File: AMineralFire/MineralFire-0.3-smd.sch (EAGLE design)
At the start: 86 parts, among them IC1 LM358, Q1 20MHz, Q2 20MHz, Q3 2N3906, Q4 2N3906, Q5 2N3906, Q6 2N3906, Q7 2N3906, Q8 2N3906, Q9 2N3906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

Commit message: Updated to almost all SMD
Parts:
- removed IC1: LM358, SparkFun-IC-Amplifiers:LM358
- removed V1: 7409N, 74ttl-din:7409N
- added IC2: 74LS09D, 74xx-eu:74LS09D
- added IC3: LM358D, linear:LM358D
- C14, C6: device rcl:C-EU075-032X103 -> rcl:C-USC0805K
- C4, C5, C7: device SparkFun-Capacitors:10UF-POLAR-RADIAL-2.5MM-25V-20% -> rcl:CPOL-US153CLV-0505
- D1, D2, D3, D4: device SparkFun-DiscreteSemi:DIODE-1N4148 -> adafruit:DIODESMA
- Q1, Q2: device adafruit:CRYSTALHC49U70 -> adafruit:CRYSTALHC49UP
- Q3, Q4, Q5, Q6, Q7, Q8, Q9: value 2N3906 -> MMBT3906LT1SMD; device transistor-pnp:2N3906 -> transistor-pnp:MMBT3906LT1SMD
- T1, T2, T3, T4, T5: device SparkFun-DiscreteSemi:TRANS_NPN-2N3904 -> transistor:MMBT3904LT1-NPN-SOT23-BEC
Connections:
- net +12V: no longer IC1G3.P$V+
- net +5V: now also IC2P.VCC, IC3P.V+; no longer V1/+UB.+UB
- net BUTLED: now also IC3B.-IN; no longer IC1G2.+IN
- net GND: now also IC2P.GND, IC3P.V-; no longer IC1G3.P$V-, V1/-UB.-UB
- net LBUTTON: now also IC2A.I1; no longer V1/1.B
- net LTRIG: now also IC2A.I0; no longer V1/1.A
- net N$19: now also IC3B.OUT; no longer IC1G2.OUT
- net N$24: now also IC3B.+IN; no longer IC1G2.-IN
- net N$32: now also IC3A.+IN; no longer IC1G1.-IN
- net N$33: now also IC3A.OUT; no longer IC1G1.OUT
- net TRIG: now also IC2A.O; no longer V1/1.Y
- net TRIGO: now also IC3A.-IN; no longer IC1G1.+IN

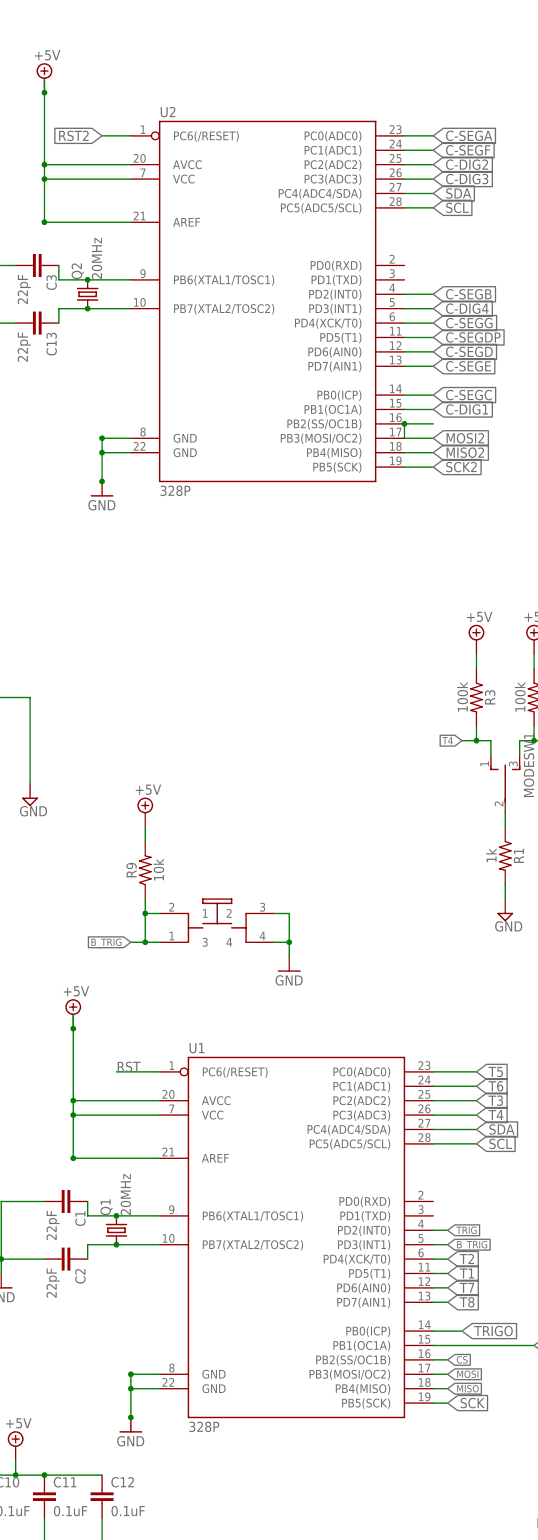
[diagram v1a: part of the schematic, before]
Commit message: 0.3-smd nor fully smd
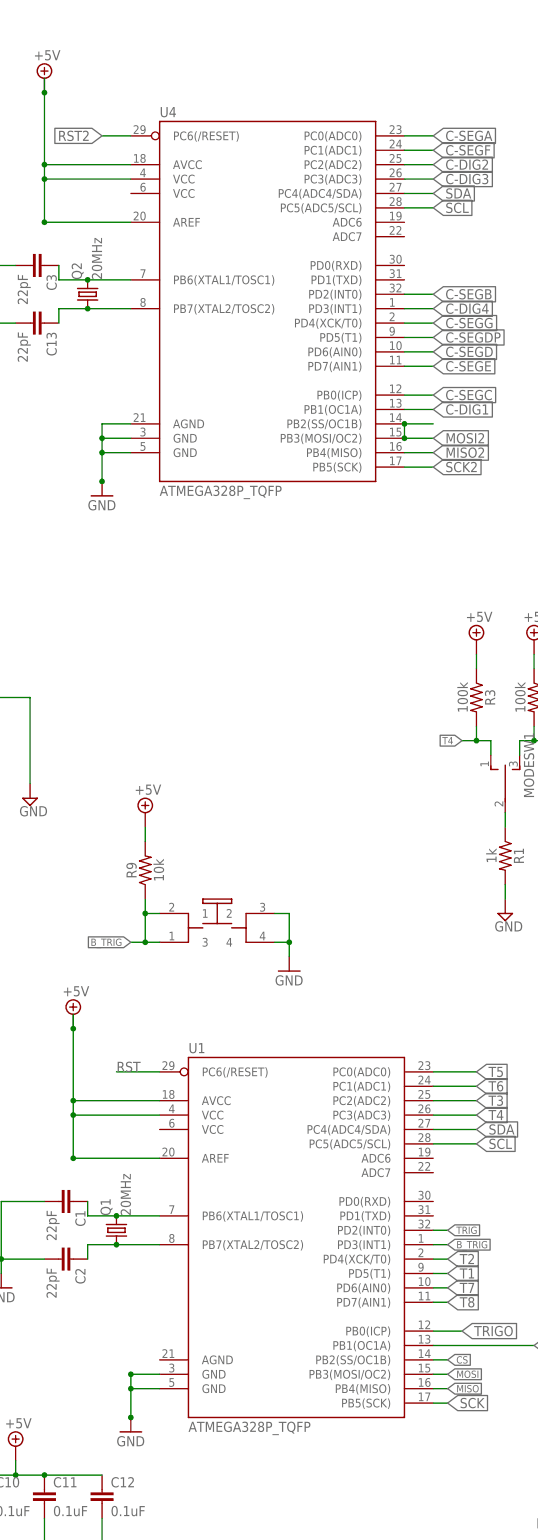
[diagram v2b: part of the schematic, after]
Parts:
- removed U2: 328P, SparkFun-IC-Microcontroller:ATMEGA328P_PDIP
- added U4: ATMEGA328P_TQFP, SparkFun-IC-Microcontroller:ATMEGA328P_TQFP
- U1: value 328P -> ATMEGA328P_TQFP; device SparkFun-IC-Microcontroller:ATMEGA328P_PDIP -> SparkFun-IC-Microcontroller:ATMEGA328P_TQFP
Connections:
- net +5V: now also U1.VCC@4, U4.AREF, U4.AVCC, U4.VCC@4; no longer U1.VCC, U2.AREF, U2.AVCC, U2.VCC
- net C-DIG1: now also U4.PB1(OC1A); no longer U2.PB1(OC1A)
- net C-DIG2: now also U4.PC2(ADC2); no longer U2.PC2(ADC2)
- net C-DIG3: now also U4.PC3(ADC3); no longer U2.PC3(ADC3)
- net C-DIG4: now also U4.PD3(INT1); no longer U2.PD3(INT1)
- net C-SEGA: now also U4.PC0(ADC0); no longer U2.PC0(ADC0)
- net C-SEGB: now also U4.PD2(INT0); no longer U2.PD2(INT0)
- net C-SEGC: now also U4.PB0(ICP); no longer U2.PB0(ICP)
- net C-SEGD: now also U4.PD6(AIN0); no longer U2.PD6(AIN0)
- net C-SEGDP: now also U4.PD5(T1); no longer U2.PD5(T1)
- net C-SEGE: now also U4.PD7(AIN1); no longer U2.PD7(AIN1)
- net C-SEGF: now also U4.PC1(ADC1); no longer U2.PC1(ADC1)
- net C-SEGG: now also U4.PD4(XCK/T0); no longer U2.PD4(XCK/T0)
- net GND: now also U1.GND@3, U1.GND@5, U4.AGND, U4.GND@3, U4.GND@5; no longer U1.GND@1, U1.GND@2, U2.GND@1, U2.GND@2
- net MISO2: now also U4.PB4(MISO); no longer U2.PB4(MISO)
- net MOSI2: now also U4.PB2(SS/OC1B), U4.PB3(MOSI/OC2); no longer U2.PB2(SS/OC1B), U2.PB3(MOSI/OC2)
- net N$7: now also U4.PB6(XTAL1/TOSC1); no longer U2.PB6(XTAL1/TOSC1)
- net N$8: now also U4.PB7(XTAL2/TOSC2); no longer U2.PB7(XTAL2/TOSC2)
- net RST2: now also U4.PC6(/RESET); no longer U2.PC6(/RESET)
- net SCK2: now also U4.PB5(SCK); no longer U2.PB5(SCK)
- net SCL: now also U4.PC5(ADC5/SCL); no longer U2.PC5(ADC5/SCL)
- net SDA: now also U4.PC4(ADC4/SDA); no longer U2.PC4(ADC4/SDA)

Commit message: Added pull up resistors on I2C comms
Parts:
- added R36, R37: 4k7, SparkFun-Resistors:1KOHM-0603-1/10W-1%
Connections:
- net +5V: now also R36.1, R37.1
- net SCL: now also R37.2
- net SDA: now also R36.2
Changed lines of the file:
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@@
 <part name="U4" library="SparkFun-IC-Microcontroller" deviceset="ATMEGA328P_TQFP" device="" value="ATMEGA328P_TQFP"/>
 <part name="U1" library="SparkFun-IC-Microcontroller" deviceset="ATMEGA328P_TQFP" device="" value="ATMEGA328P_TQFP"/>
+<part name="R36" library="SparkFun-Resistors" deviceset="1KOHM" device="-0603-1/10W-1%" value="4k7"/>
+<part name="R37" library="SparkFun-Resistors" deviceset="1KOHM" device="-0603-1/10W-1%" value="4k7"/>
+<part name="SUPPLY23" library="supply2" deviceset="+5V" device=""/>
+<part name="SUPPLY44" library="supply2" deviceset="+5V" device=""/>
 </parts>
 <sheets>
@@
 <instance part="U4" gate="U$1" x="83.82" y="203.2"/>
 <instance part="U1" gate="U$1" x="88.9" y="38.1"/>
+<instance part="R36" gate="G$1" x="147.32" y="60.96" rot="R270"/>
+<instance part="R37" gate="G$1" x="160.02" y="60.96" rot="R270"/>
+<instance part="SUPPLY23" gate="+5V" x="147.32" y="76.2"/>
+<instance part="SUPPLY44" gate="+5V" x="160.02" y="76.2"/>
 </instances>
 <busses>
@@
 <pinref part="SUPPLY22" gate="+5V" pin="+5V"/>
 </segment>
+<segment>
+<pinref part="SUPPLY23" gate="+5V" pin="+5V"/>
+<pinref part="R36" gate="G$1" pin="1"/>
+<wire x1="147.32" y1="73.66" x2="147.32" y2="66.04" width="0.1524" layer="91"/>
+</segment>
+<segment>
+<pinref part="SUPPLY44" gate="+5V" pin="+5V"/>
+<pinref part="R37" gate="G$1" pin="1"/>
+<wire x1="160.02" y1="73.66" x2="160.02" y2="66.04" width="0.1524" layer="91"/>
+</segment>
 </net>
 <net name="MISO" class="0">
@@
 <pinref part="U4" gate="U$1" pin="PC4(ADC4/SDA)"/>
 </segment>
+<segment>
+<pinref part="R36" gate="G$1" pin="2"/>
+<wire x1="147.32" y1="55.88" x2="147.32" y2="50.8" width="0.1524" layer="91"/>
+<label x="147.32" y="50.8" size="1.778" layer="95" rot="R180" xref="yes"/>
+</segment>
 </net>
 <net name="SCL" class="0">
@@
 <pinref part="U4" gate="U$1" pin="PC5(ADC5/SCL)"/>
 </segment>
-</net>
+<segment>
+<pinref part="R37" gate="G$1" pin="2"/>
+<wire x1="160.02" y1="55.88" x2="160.02" y2="50.8" width="0.1524" layer="91"/>
+<label x="160.02" y="50.8" size="1.778" layer="95" rot="R180" xref="yes"/>
+</segment>
+</net>
